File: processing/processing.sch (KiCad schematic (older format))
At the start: 26 parts, among them J1 HRO-TYPE-C-31-M-12, J2 Conn_01x03, J3 ICSP, SW1 SW_RESET, U1 CH340G, U2 ATmega328P-AU, Y1 12MHz, Y2 16MHz

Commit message: base audio board
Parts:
- R3, R4: footprint Resistor_SMD:R_1206_3216Metric -> Resistor_SMD:R_0603_1608Metric
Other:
- moved on the sheet: C7, R6, SW1
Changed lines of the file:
@@
 	0    -1   -1   0
 $EndComp
-Wire Wire Line
-	8550 4100 9050 4100
-Wire Wire Line
-	9050 4100 9500 4100
-Connection ~ 9500 4100
-Wire Wire Line
-	9500 4100 9600 4100
-Wire Wire Line
-	9500 4200 9500 4100
-Text GLabel 9600 4100 2    50   Input ~ 0
+Connection ~ 9550 4100
+Wire Wire Line
+	9550 4200 9550 4100
+Text GLabel 9650 4100 2    50   Input ~ 0
 RESET
 $Comp
 L Device:C_Small C7
 U 1 1 60592AFD
-P 9050 4300
-F 0 "C7" H 9142 4346 50  0000 L CNN
-F 1 "100nF" H 9142 4255 50  0000 L CNN
-F 2 "Capacitor_SMD:C_0603_1608Metric" H 9050 4300 50  0001 C CNN
-F 3 "~" H 9050 4300 50  0001 C CNN
-	1    9050 4300
-	1    0    0    -1
-$EndComp
-Text GLabel 9050 4400 3    50   Input ~ 0
+P 9100 4300
+F 0 "C7" H 9192 4346 50  0000 L CNN
+F 1 "100nF" H 9192 4255 50  0000 L CNN
+F 2 "Capacitor_SMD:C_0603_1608Metric" H 9100 4300 50  0001 C CNN
+F 3 "~" H 9100 4300 50  0001 C CNN
+	1    9100 4300
+	1    0    0    -1
+$EndComp
+Text GLabel 9100 4400 3    50   Input ~ 0
 ~DTR
 $Comp
 L Switch:SW_Push SW1
 U 1 1 605744B8
-P 9500 4400
-F 0 "SW1" V 9454 4548 50  0000 L CNN
-F 1 "SW_RESET" V 9545 4548 50  0000 L CNN
-F 2 "Button_Switch_SMD:SW_SPST_SKQG_WithoutStem" H 9500 4600 50  0001 C CNN
-F 3 "~" H 9500 4600 50  0001 C CNN
-	1    9500 4400
+P 9550 4400
+F 0 "SW1" V 9504 4548 50  0000 L CNN
+F 1 "SW_RESET" V 9595 4548 50  0000 L CNN
+F 2 "Button_Switch_SMD:SW_SPST_SKQG_WithoutStem" H 9550 4600 50  0001 C CNN
+F 3 "~" H 9550 4600 50  0001 C CNN
+	1    9550 4400
 	0    1    1    0
 $EndComp
@@
 L power:GND #PWR020
 U 1 1 605B0D83
-P 9500 4600
-F 0 "#PWR020" H 9500 4350 50  0001 C CNN
-F 1 "GND" H 9505 4427 50  0000 C CNN
-F 2 "" H 9500 4600 50  0001 C CNN
-F 3 "" H 9500 4600 50  0001 C CNN
-	1    9500 4600
-	1    0    0    -1
-$EndComp
-Wire Wire Line
-	9050 4200 9050 4100
-Connection ~ 9050 4100
-Wire Wire Line
-	9050 4100 9050 4000
+P 9550 4600
+F 0 "#PWR020" H 9550 4350 50  0001 C CNN
+F 1 "GND" H 9555 4427 50  0000 C CNN
+F 2 "" H 9550 4600 50  0001 C CNN
+F 3 "" H 9550 4600 50  0001 C CNN
+	1    9550 4600
+	1    0    0    -1
+$EndComp
+Wire Wire Line
+	9100 4200 9100 4100
+Connection ~ 9100 4100
+Wire Wire Line
+	9100 4100 9100 4000
 $Comp
 L power:+5V #PWR016
 U 1 1 605738B3
-P 9050 3800
-F 0 "#PWR016" H 9050 3650 50  0001 C CNN
-F 1 "+5V" H 9065 3973 50  0000 C CNN
-F 2 "" H 9050 3800 50  0001 C CNN
-F 3 "" H 9050 3800 50  0001 C CNN
-	1    9050 3800
+P 9100 3800
+F 0 "#PWR016" H 9100 3650 50  0001 C CNN
+F 1 "+5V" H 9115 3973 50  0000 C CNN
+F 2 "" H 9100 3800 50  0001 C CNN
+F 3 "" H 9100 3800 50  0001 C CNN
+	1    9100 3800
 	1    0    0    -1
 $EndComp
@@
 L Device:R_Small R6
 U 1 1 60572FD6
-P 9050 3900
-F 0 "R6" H 9109 3946 50  0000 L CNN
-F 1 "10k" H 9109 3855 50  0000 L CNN
-F 2 "Resistor_SMD:R_1206_3216Metric" H 9050 3900 50  0001 C CNN
-F 3 "~" H 9050 3900 50  0001 C CNN
-	1    9050 3900
+P 9100 3900
+F 0 "R6" H 9159 3946 50  0000 L CNN
+F 1 "10k" H 9159 3855 50  0000 L CNN
+F 2 "Resistor_SMD:R_1206_3216Metric" H 9100 3900 50  0001 C CNN
+F 3 "~" H 9100 3900 50  0001 C CNN
+	1    9100 3900
 	1    0    0    -1
 $EndComp
@@
 F 0 "R3" H 6909 2446 50  0000 L CNN
 F 1 "12k" H 6909 2355 50  0000 L CNN
-F 2 "Resistor_SMD:R_1206_3216Metric" H 6850 2400 50  0001 C CNN
+F 2 "Resistor_SMD:R_0603_1608Metric" H 6850 2400 50  0001 C CNN
 F 3 "~" H 6850 2400 50  0001 C CNN
 	1    6850 2400
@@
 F 0 "R4" H 6909 2846 50  0000 L CNN
 F 1 "8.2k" H 6909 2755 50  0000 L CNN
-F 2 "Resistor_SMD:R_1206_3216Metric" H 6850 2800 50  0001 C CNN
+F 2 "Resistor_SMD:R_0603_1608Metric" H 6850 2800 50  0001 C CNN
 F 3 "~" H 6850 2800 50  0001 C CNN
 	1    6850 2800
@@
 	1    0    0    -1
 $EndComp
+Wire Wire Line
+	9550 4100 9650 4100
+Wire Wire Line
+	9100 4100 9550 4100
+Wire Wire Line
+	8550 4100 9100 4100
 $EndSCHEMATC

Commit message: finish the processing board
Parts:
- added J1: Conn_01x02, Connector_PinSocket_2.54mm:PinSocket_1x02_P2.54mm_Vertical, symbol Connector_Generic:Conn_01x02
- added J3: Conn_01x05, Connector_PinSocket_2.54mm:PinSocket_1x05_P2.54mm_Vertical, symbol Connector_Generic:Conn_01x05
- J2: footprint Connector_PinHeader_2.54mm:PinHeader_1x03_P2.54mm_Vertical -> Connector_PinSocket_2.54mm:PinSocket_1x03_P2.54mm_Vertical
- renumbered J1 to J4, J3 to J5
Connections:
- net A3 is gone; now on net A2: J2.3 (Pin_3)
- net +5V: now also J1.1 (Pin_1)
- net GND: now also J1.2 (Pin_2)
- net D2: now reaches U2.1 (PD3)
- net D2: now also J3.2 (Pin_2)
- net D5: now reaches U2.10 (PD6)
- net D5: now also J3.5 (Pin_5)
- net D3: now reaches U2.2 (PD4)
- net D3: now also J3.3 (Pin_3)
- net D1: now reaches U2.32 (PD2)
- net D1: now also J3.1 (Pin_1)
- net D4: now reaches U2.9 (PD5)
- net D4: now also J3.4 (Pin_4)
- no-connect marks 17 -> 18
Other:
- moved on the sheet: C1, C10, C2, C3, C4, C5, C6, C7, C8, C9, F1, J2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

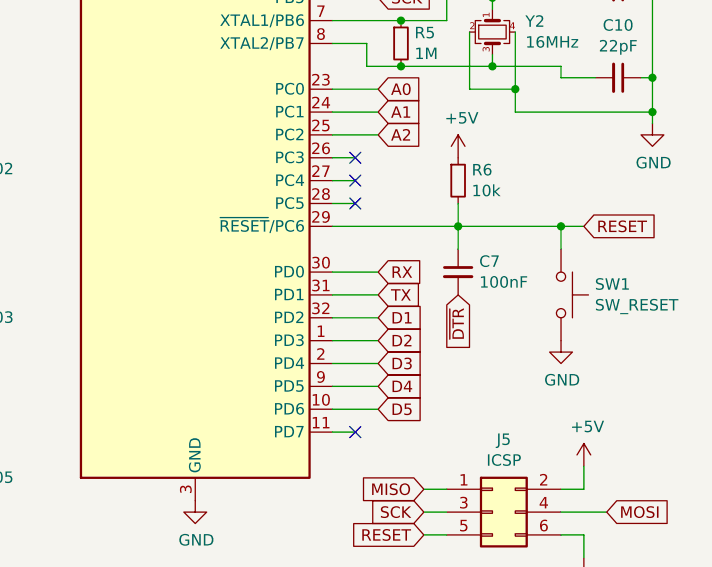
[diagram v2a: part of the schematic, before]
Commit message: errata 1: rx and tx are flipped
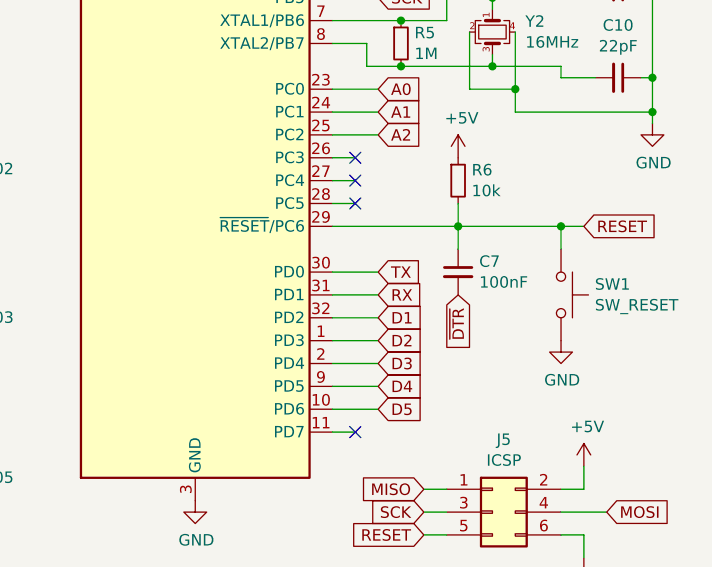
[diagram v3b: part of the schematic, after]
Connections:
- net RX: now also U2.31 (PD1); no longer U2.30 (PD0)
- net TX: now also U2.30 (PD0); no longer U2.31 (PD1)
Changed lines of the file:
@@
 Wire Wire Line
 	8400 3800 8500 3800
+Text GLabel 8600 4300 2    50   Input ~ 0
+TX
 Text GLabel 8600 4400 2    50   Input ~ 0
-TX
-Text GLabel 8600 4300 2    50   Input ~ 0
 RX
 Wire Wire Line

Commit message: errata 2: fix footprints
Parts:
- J1: footprint Connector_PinSocket_2.54mm:PinSocket_1x02_P2.54mm_Vertical -> df-parts:310-XX-102-41-001000
- J2: footprint Connector_PinSocket_2.54mm:PinSocket_1x03_P2.54mm_Vertical -> df-parts:310-XX-103-41-001000
- J3: footprint Connector_PinSocket_2.54mm:PinSocket_1x05_P2.54mm_Vertical -> df-parts:310-XX-105-41-001000
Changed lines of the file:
@@
 F 0 "J2" H 6580 4492 50  0000 L CNN
 F 1 "Conn_01x03" H 6580 4401 50  0000 L CNN
-F 2 "Connector_PinSocket_2.54mm:PinSocket_1x03_P2.54mm_Vertical" H 6500 4450 50  0001 C CNN
+F 2 "df-parts:310-XX-103-41-001000" H 6500 4450 50  0001 C CNN
 F 3 "~" H 6500 4450 50  0001 C CNN
 	1    6500 4450
@@
 F 0 "J1" H 6580 3742 50  0000 L CNN
 F 1 "Conn_01x02" H 6580 3651 50  0000 L CNN
-F 2 "Connector_PinSocket_2.54mm:PinSocket_1x02_P2.54mm_Vertical" H 6500 3750 50  0001 C CNN
+F 2 "df-parts:310-XX-102-41-001000" H 6500 3750 50  0001 C CNN
 F 3 "~" H 6500 3750 50  0001 C CNN
 	1    6500 3750
@@
 F 0 "J3" H 6580 5192 50  0000 L CNN
 F 1 "Conn_01x05" H 6580 5101 50  0000 L CNN
-F 2 "Connector_PinSocket_2.54mm:PinSocket_1x05_P2.54mm_Vertical" H 6500 5150 50  0001 C CNN
+F 2 "df-parts:310-XX-105-41-001000" H 6500 5150 50  0001 C CNN
 F 3 "~" H 6500 5150 50  0001 C CNN
 	1    6500 5150
